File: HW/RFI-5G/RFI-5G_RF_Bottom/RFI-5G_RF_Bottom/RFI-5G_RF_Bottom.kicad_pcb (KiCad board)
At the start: 2 copper layers, 40 x 40 mm, 8 parts, among them J1 CES-110-XX-Y-S, J2 CES-110-XX-Y-S, J3 CES-110-XX-Y-S, J4 CES-110-XX-Y-S

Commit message: RF top and Bottom boards
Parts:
- removed the ? at (128.3, 79.9)
- removed the ? at (161.3, 112.9)
- removed the ? at (161.3, 79.9)
- removed the ? at (128.3, 112.9)
- added ?: , , F.Cu at (121.5, 109.5)
- added ?: , , F.Cu at (154.5, 109.5)
- added ?: , , F.Cu at (154.5, 76.5)
- added ?: , AutoGenerated:MountingHole_3.50mm, F.Cu at (121.5, 76.5)
- added C1: 100nF, Capacitor_SMD:C_0402_1005Metric, F.Cu at (134.6, 86.7)
- added C10: 1uF, Capacitor_SMD:C_0402_1005Metric, F.Cu at (154.2, 101.9)
- added C11: 10nF, Capacitor_SMD:C_0402_1005Metric, F.Cu at (153.1, 101.9)
- added C12: 10nF, Capacitor_SMD:C_0402_1005Metric, F.Cu at (137.8, 95.3)
- added C13: C, Capacitor_SMD:C_0402_1005Metric, F.Cu at (151.7, 95.5)
- added C14: C, Capacitor_SMD:C_0402_1005Metric, F.Cu at (151.7, 100.4)
- added C15: 33nF, Capacitor_SMD:C_0402_1005Metric, F.Cu at (148.3, 103.3)
- added C16: C, Capacitor_SMD:C_0402_1005Metric, F.Cu at (148.4, 97.7)
- added C17: C, Capacitor_SMD:C_0402_1005Metric, F.Cu at (150.1, 100.4)
- added C18: 10uF, Capacitor_SMD:C_0402_1005Metric, F.Cu at (121.9, 104.3)
- added C2: 10nF, Capacitor_SMD:C_0402_1005Metric, F.Cu at (134.6, 87.9)
- added C4: 10nF, Capacitor_SMD:C_0402_1005Metric, F.Cu at (133.2, 83.2)
- added C5: 100nF, Capacitor_SMD:C_0402_1005Metric, F.Cu at (142.0, 87.9)
- added C6: 1uF, Capacitor_SMD:C_0402_1005Metric, F.Cu at (138.4, 99.6)
- added C7: 10nF, Capacitor_SMD:C_0402_1005Metric, F.Cu at (137.3, 99.6)
- added C8: 1uF, Capacitor_SMD:C_0402_1005Metric, F.Cu at (143.1, 99.6)
- added C9: 10nF, Capacitor_SMD:C_0402_1005Metric, F.Cu at (142.0, 99.6)
- added FL1: LFCW-8400+, GGS_RF:JC0603C-1, F.Cu at (129.5, 83.3)
- added FL2: HFCN-5500+, GGS_RF:JC0603C, F.Cu at (142.7, 83.6)
- added FL3: SAW_869, GGS_RF:QCS5P, F.Cu at (139.1, 95.9)
- added J5: SMP, GGS_Connectors:SMP_StraightPlugPCB, F.Cu at (148.8, 83.2)
- added J6: Conn_01x06_Female, Connector_PinHeader_1.00mm:PinHeader_1x06_P1.00mm_Vertical, F.Cu at (136.4, 91.3)
- added L1: 0.9uH, Inductor_SMD:L_0603_1608Metric, F.Cu at (135.1, 84.0)
- added L2: 590nH, Inductor_SMD:L_0603_1608Metric, F.Cu at (140.2, 84.0)
- added L3: 120nH, Inductor_SMD:L_0603_1608Metric, F.Cu at (135.9, 96.2)
- added L4: 120nH, Inductor_SMD:L_0603_1608Metric, F.Cu at (144.5, 95.9)
- added L5: L, Inductor_SMD:L_0603_1608Metric, F.Cu at (150.9, 97.2)
- added R1: 3k, Resistor_SMD:R_0603_1608Metric, F.Cu at (138.6, 87.1)
- added R2: 43R, Resistor_SMD:R_0603_1608Metric, F.Cu at (140.2, 87.1)
- added R3: 88R7, Resistor_SMD:R_0603_1608Metric, F.Cu at (135.9, 99.2)
- added R4: 88R7, Resistor_SMD:R_0603_1608Metric, F.Cu at (144.5, 99.2)
- added R5: R, Resistor_SMD:R_0603_1608Metric, F.Cu at (150.9, 98.7)
- added U1: HMC8411, GGS_RF:6-LFCSP, F.Cu at (141.9, 81.9)
- added U2: SIM-14+, GGS_RF:HV1195, F.Cu at (125.6, 94.7)
- added U3: LT5537, Package_DFN_QFN:DFN-8-1EP_2x3mm_P0.5mm_EP0.56x2.15mm, F.Cu at (150.8, 103.3)
- added U4: LEE2-6+, Package_SON:WSON-6-1EP_2x2mm_P0.65mm_EP1x1.6mm, F.Cu at (133.6, 95.3)
- added U5: LEE2-6+, Package_SON:WSON-6-1EP_2x2mm_P0.65mm_EP1x1.6mm, F.Cu at (142.2, 95.1)
- added U7: HMC358, Package_SO:MSOP-8-1EP_3x3mm_P0.65mm_EP2.5x3mm_Mask1.73x2.36mm, F.Cu at (124.3, 102.6)
- J1, J3: value CES-110-XX-Y-S -> Conn_01x03; footprint easyeda:CES-110-XX-Y-S -> Connector_PinHeader_2.54mm:PinHeader_1x03_P2.54mm_Vertical
- J2: value CES-110-XX-Y-S -> Conn_01x02; footprint easyeda:CES-110-XX-Y-S -> Connector_PinHeader_2.54mm:PinHeader_1x02_P2.54mm_Vertical
- J4: value CES-110-XX-Y-S -> Conn_01x10; footprint easyeda:CES-110-XX-Y-S -> Connector_PinHeader_2.54mm:PinHeader_1x10_P2.54mm_Vertical
- moved J3 33.5 mm to (121.5, 81.6)
- moved J4 24.6 mm to (126.6, 109.5), turned to 90 degrees
- moved J2 16.7 mm to (146.9, 76.5), turned to 90 degrees
- moved J1 7.63 mm to (126.6, 76.5), turned to 90 degrees
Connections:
- J1 pad 1: (no net) -> SDA
- J1 pad 2: (no net) -> SCL
- J1 pad 3: (no net) -> GND
- J2 pad 1: (no net) -> GND
- J2 pad 2: (no net) -> VCC
- J3 pad 1: (no net) -> GND
- J3 pad 2: (no net) -> ADC_PL2
- J3 pad 3: (no net) -> DAC_PL2
- J4 pad 1: (no net) -> Vcc_VCO
- J4 pad 10: (no net) -> GND
- J4 pad 2: (no net) -> VTune2
- J4 pad 3: (no net) -> GND
- J4 pad 4: (no net) -> GND
- J4 pad 5: (no net) -> PoL
- J4 pad 6: (no net) -> Vcc_IF2Amp1
- J4 pad 7: (no net) -> Vcc_IF2Amp2
- J4 pad 8: (no net) -> 3V
- J4 pad 9: (no net) -> RSSI_Out
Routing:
- net 3V: track 0.00 -> 22.8 mm, vias 0 -> 2
- net GND: track 0.00 -> 17.4 mm, vias 0 -> 13
- net Vcc_IF2Amp2: track 0.00 -> 13.6 mm
- net Vcc_IF2Amp1: track 0.00 -> 13.2 mm
- net Vcc_IF1Amp: track 0.00 -> 10.1 mm
- net IF1_Out: track 0.00 -> 9.62 mm
- net Vcc_VCO: track 0.00 -> 8.90 mm
- net /LEE_2_Out: track 0.00 -> 8.44 mm
- net RSSI_Out: track 0.00 -> 8.39 mm
- net VTune2: track 0.00 -> 7.87 mm
- net /Mixer_Out: track 0.00 -> 4.84 mm
- net Net-(C16-Pad2): track 0.00 -> 4.40 mm
- net Net-(C13-Pad2): track 0.00 -> 3.94 mm
- net LO2: track 0.00 -> 3.82 mm
- net IF1_In: track 0.00 -> 3.18 mm
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- added copper zone on B.Cu, net GND
- added copper zone on F.Cu, net GND
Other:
- outline, holes or cut-outs redrawn
- board text added: "RO4350B thickness = 0.3 mm Er = 3.66 tand = 37e-4"
- board text removed: "BOTTOM"
- board text removed: "TOP"

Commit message: PL boards
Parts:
- J6: value Conn_01x06_Female -> Conn_01x10_Female; footprint Connector_PinHeader_1.00mm:PinHeader_1x06_P1.00mm_Vertical -> Connector_PinHeader_1.00mm:PinHeader_1x10_P1.00mm_Vertical
- moved J6 2.00 mm to (134.4, 91.3)
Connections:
- J6 pad 1: VTune1 -> Vcc_IF1Amp
- J6 pad 2: Vcc_LO1Amp -> VTune1
- J6 pad 3: Vcc_IF1Amp -> Vcc_VCO
- J6 pad 4: Vcc_LNA1 -> Vcc_LO1Amp
- J6 pad 6: Vcc_VCO -> Vcc_LNA1
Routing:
- net Vcc_VCO: track 8.90 -> 9.78 mm
- net Vcc_IF1Amp: track 10.1 -> 10.7 mm
- net VTune2: track 7.87 -> 8.41 mm

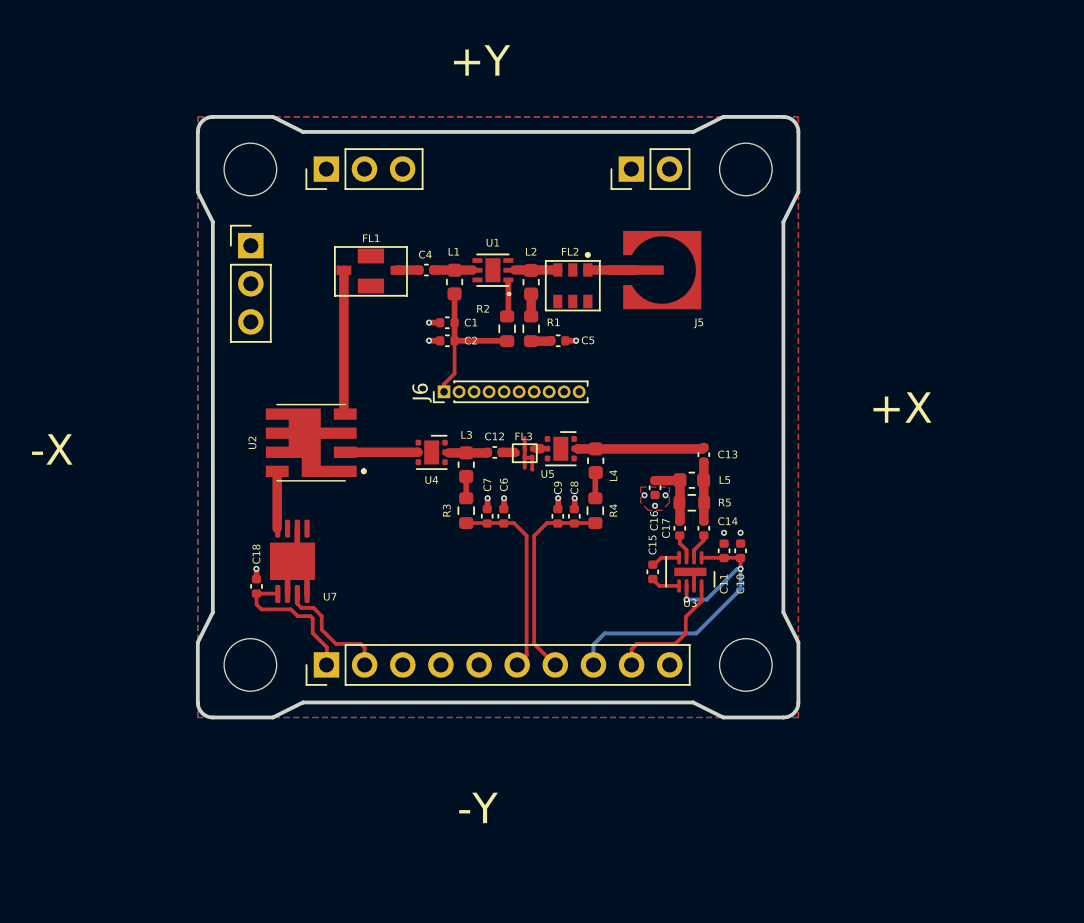
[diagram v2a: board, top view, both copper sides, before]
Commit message: All boards dseigned, thickness change pending
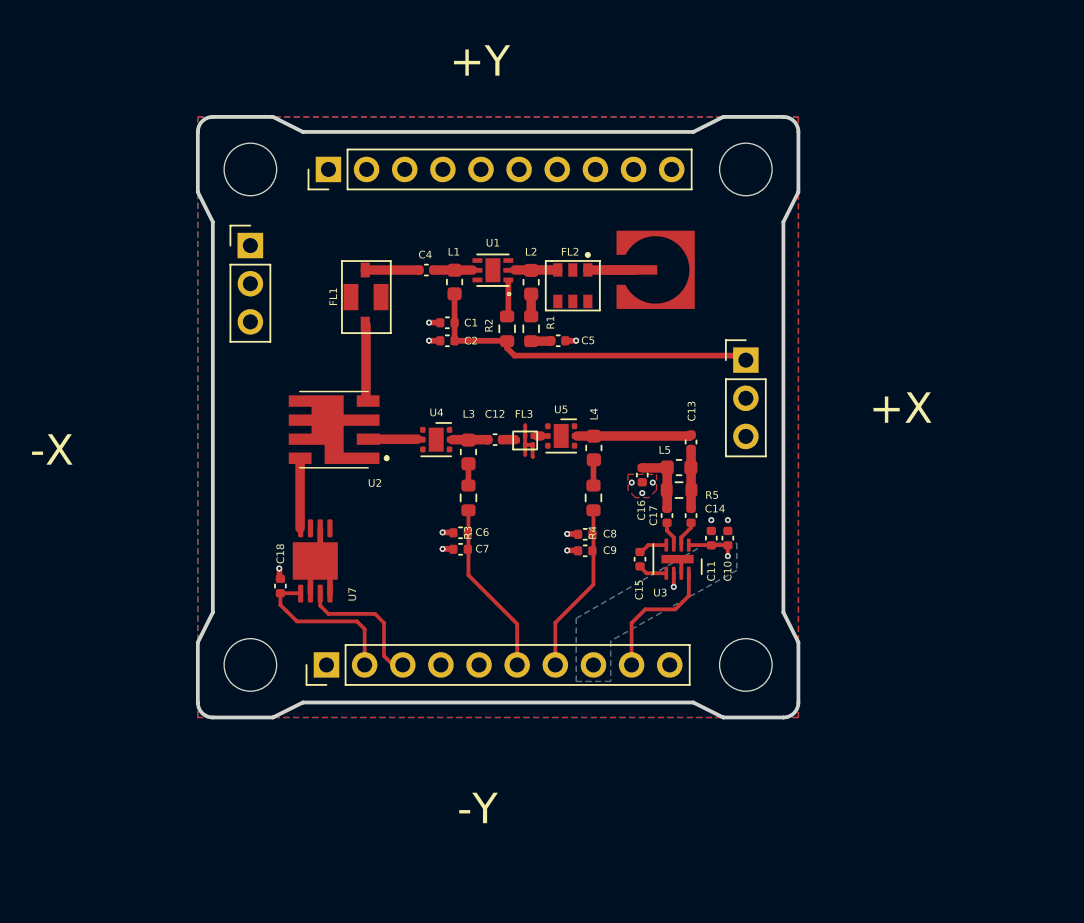
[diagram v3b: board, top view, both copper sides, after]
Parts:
- removed J6: Conn_01x10_Female, Connector_PinHeader_1.00mm:PinHeader_1x10_P1.00mm_Vertical
- J1: value Conn_01x03 -> Conn_01x10; footprint Connector_PinHeader_2.54mm:PinHeader_1x03_P2.54mm_Vertical -> Connector_PinHeader_2.54mm:PinHeader_1x10_P2.54mm_Vertical
- J2: value Conn_01x02 -> Conn_01x03; footprint Connector_PinHeader_2.54mm:PinHeader_1x02_P2.54mm_Vertical -> Connector_PinHeader_2.54mm:PinHeader_1x03_P2.54mm_Vertical
- moved J2 14.8 mm to (154.5, 89.2), turned to 0 degrees
- moved C6 3.08 mm to (135.5, 100.7), turned to 0 degrees
- moved C9 2.94 mm to (143.8, 101.9), turned to 0 degrees
- moved C7 2.83 mm to (135.5, 101.8), turned to 0 degrees
- moved FL1 1.77 mm to (129.2, 85.0), turned to -90 degrees
- moved U2 1.76 mm to (127.1, 93.8)
- moved C18 1.59 mm to (123.5, 104.2)
- moved U7 1.53 mm to (125.8, 102.6)
- moved C8 1.40 mm to (143.8, 100.8), turned to 0 degrees
- moved C11 1.20 mm to (152.2, 101.1)
- moved C15 1.20 mm to (147.4, 102.5)
- moved U3 1.20 mm to (150.0, 102.5)
- moved C10 1.20 mm to (153.3, 101.1)
- moved C14 1.20 mm to (150.8, 99.6)
- moved C17 1.20 mm to (149.2, 99.6)
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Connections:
- J2 pad 1: GND -> Vcc_IF1Amp
- J2 pad 2: VCC -> Vcc_LNA2
- J3 pad 1: GND -> 3V
- J4 pad 1: Vcc_VCO -> VTune1
- J4 pad 2: VTune2 -> Vcc_VCO
- J4 pad 3: GND -> VTune2
- J4 pad 4: GND -> Vcc_LO1Amp
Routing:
- net 3V: track 22.8 -> 4.21 mm
- net Vcc_IF1Amp: track 10.7 -> 23.3 mm
- net IF1_Out: track 9.62 -> 4.93 mm
- net Vcc_IF2Amp2: track 13.6 -> 11.4 mm
- net /IF1_LPF_In: track 1.42 -> 3.59 mm
- net /Mixer_Out: track 4.84 -> 3.09 mm
- net Vcc_IF2Amp1: track 13.2 -> 11.6 mm
- net Vcc_VCO: track 9.78 -> 10.8 mm
- net LO2: track 3.82 -> 4.67 mm
- net VTune2: track 8.41 -> 9.22 mm
- net /LEE_2_Out: track 8.44 -> 7.63 mm
- added copper zone on B.Cu, net 3V

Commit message: almost finished PCB's
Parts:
- moved C7 0.10 mm to (135.5, 101.9)
- moved C8 0.10 mm to (143.8, 100.7)
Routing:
- net GND: track 17.4 -> 16.9 mm, vias 13 -> 24
